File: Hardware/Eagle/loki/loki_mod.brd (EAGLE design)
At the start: 21.9 x 22.9 mm, 39 parts

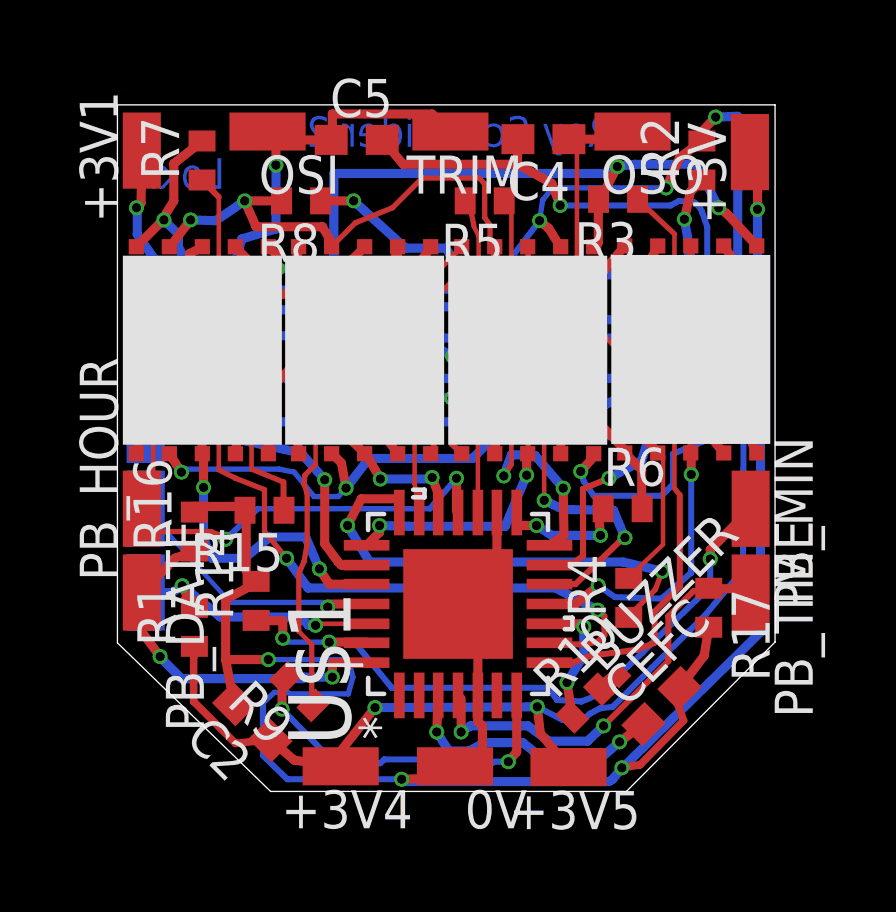
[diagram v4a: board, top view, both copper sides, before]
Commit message: Optimized layout and Litronix display footprint.
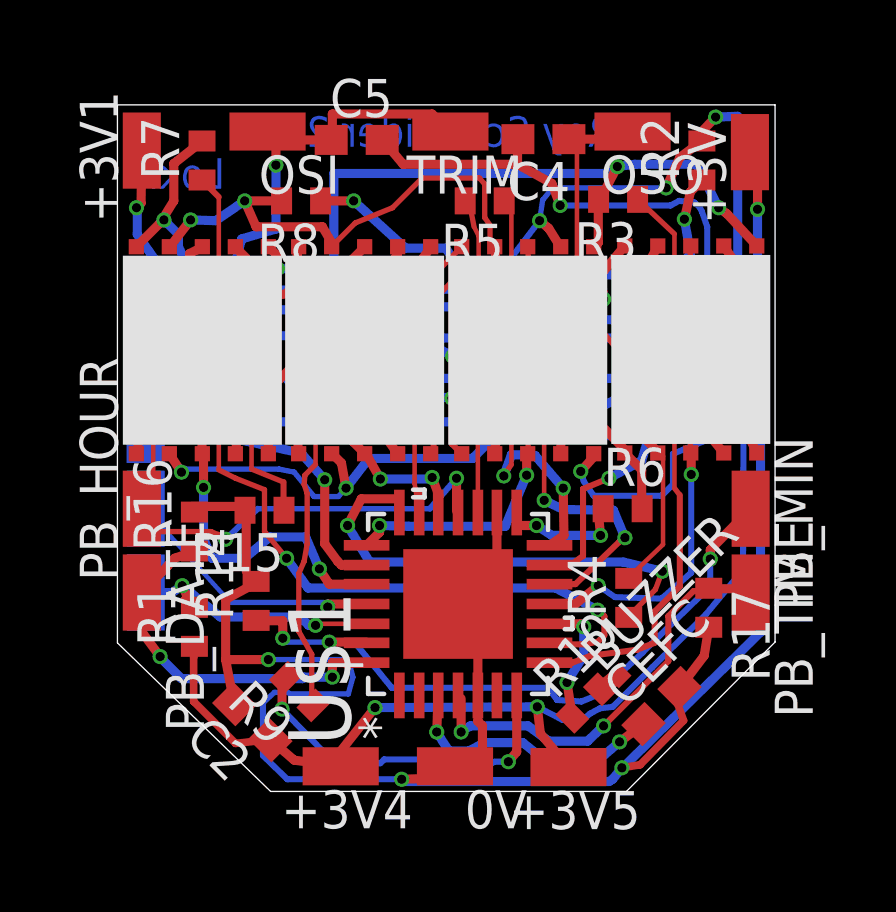
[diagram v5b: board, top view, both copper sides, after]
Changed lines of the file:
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@@
 <contactref element="PAD2" pad="1"/>
 <wire x1="6.985" y1="6.096" x2="8.2804" y2="6.096" width="0.3048" layer="1"/>
-<wire x1="6.985" y1="5.9944" x2="6.985" y2="6.096" width="0.1524" layer="1"/>
+<wire x1="6.985" y1="5.9944" x2="6.985" y2="6.096" width="0.3048" layer="1"/>
 <wire x1="6.8326" y1="6.1468" x2="6.985" y2="5.9944" width="0.1778" layer="16"/>
 <wire x1="3.7338" y1="6.1468" x2="6.8326" y2="6.1468" width="0.1778" layer="16"/>
@@
 <wire x1="18.7198" y1="6.6802" x2="17.8816" y2="5.842" width="0.2032" layer="1"/>
 <wire x1="16.8402" y1="14.3256" x2="18.5166" y2="14.3256" width="0.3048" layer="16"/>
-<wire x1="15.2908" y1="16.0782" x2="16.8402" y2="14.3256" width="0.1524" layer="1"/>
-<wire x1="15.2908" y1="21.5392" x2="15.2908" y2="16.0782" width="0.1524" layer="1"/>
+<wire x1="15.2908" y1="16.2306" x2="16.8402" y2="14.3256" width="0.1778" layer="1"/>
+<wire x1="15.2908" y1="21.5392" x2="15.2908" y2="16.2306" width="0.1524" layer="1"/>
 <wire x1="15.2908" y1="21.5392" x2="15.0232" y2="21.59" width="0.1524" layer="1"/>
 <via x="18.5166" y="14.3256" extent="1-16" drill="0.3048"/>
@@
 <wire x1="11.43" y1="17.9832" x2="11.4506" y2="18.0046" width="0.1524" layer="1"/>
 <wire x1="16.1036" y1="17.0942" x2="16.8656" y2="18.0086" width="0.3048" layer="1"/>
-<wire x1="15.9258" y1="16.2052" x2="16.1036" y2="17.0942" width="0.3048" layer="1"/>
+<wire x1="16.1798" y1="16.256" x2="16.1036" y2="17.0942" width="0.3048" layer="1"/>
 <wire x1="16.8656" y1="18.0086" x2="16.8862" y2="18.03" width="0.1524" layer="1"/>
 <wire x1="9.652" y1="16.0274" x2="9.4742" y2="16.002" width="0.3048" layer="16"/>
@@
 <via x="1.524" y="18.8976" extent="1-16" drill="0.3048"/>
 <via x="9.4742" y="16.002" extent="1-16" drill="0.3048"/>
-<via x="15.9258" y="16.2052" extent="1-16" drill="0.3048"/>
+<via x="16.1798" y="16.256" extent="1-16" drill="0.3048"/>
 <wire x1="2.6162" y1="16.7132" x2="2.0066" y2="18.0086" width="0.3048" layer="16"/>
 <wire x1="2.0066" y1="18.0086" x2="2.0066" y2="18.415" width="0.3048" layer="16"/>
@@
 <wire x1="9.4742" y1="16.002" x2="8.6106" y2="15.9004" width="0.3048" layer="16"/>
 <wire x1="8.6106" y1="15.9004" x2="5.3594" y2="15.9004" width="0.3048" layer="16"/>
-<wire x1="15.9258" y1="16.2052" x2="15.0876" y2="16.3576" width="0.3048" layer="16"/>
+<wire x1="16.1798" y1="16.256" x2="15.0876" y2="16.3576" width="0.3048" layer="16"/>
 <wire x1="15.0876" y1="16.3576" x2="13.9446" y2="16.002" width="0.3048" layer="16"/>
 <wire x1="13.9446" y1="16.002" x2="9.4742" y2="16.002" width="0.3048" layer="16"/>
@@
 <wire x1="21.2852" y1="11.1506" x2="21.2862" y2="11.13" width="0.1524" layer="1"/>
 <wire x1="6.4516" y1="2.7686" x2="6.5024" y2="2.7178" width="0.1524" layer="1"/>
-<wire x1="6.4516" y1="4.7498" x2="6.4516" y2="2.7686" width="0.1778" layer="1"/>
-<wire x1="6.0198" y1="5.1816" x2="6.4516" y2="4.7498" width="0.1524" layer="1"/>
+<wire x1="6.4516" y1="4.4196" x2="6.4516" y2="2.7686" width="0.1778" layer="1"/>
+<wire x1="6.0198" y1="5.1816" x2="6.4516" y2="4.4196" width="0.1778" layer="1"/>
 <wire x1="6.0198" y1="7.112" x2="6.0198" y2="5.1816" width="0.1778" layer="1"/>
 <wire x1="6.1976" y1="7.5184" x2="6.0198" y2="7.112" width="0.1778" layer="1"/>
